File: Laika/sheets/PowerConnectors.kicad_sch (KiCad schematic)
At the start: 0 parts

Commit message: Created USB-C and XT30 Power Input Block
Created a power selection circuit that allows for providing system power
(VDD) via a USB-C receptacle (with ESD protection) or via a XT30
connector. Also attached pin headers to provide power from a bench when
doing bringup.
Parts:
- added D1, D2: D, symbol Device:D
- added J1: USB_C_Receptacle_USB2.0_16P, symbol Connector:USB_C_Receptacle_USB2.0_16P
- added J2: Conn_01x02_Socket, Connector_AMASS:AMASS_XT30PW-F_1x02_P2.50mm_Horizontal, symbol Connector:Conn_01x02_Socket
- added J3: Conn_01x02_Socket, Connector_PinHeader_1.00mm:PinHeader_1x02_P1.00mm_Vertical, symbol Connector:Conn_01x02_Socket
- added R1, R2: 5.1k, symbol Device:R
- added TP1: USB TP, TestPoint:TestPoint_Pad_1.0x1.0mm, symbol Connector:TestPoint
- added TP2: VDD TP, TestPoint:TestPoint_Pad_1.0x1.0mm, symbol Connector:TestPoint
- added TP3: VIN TP, TestPoint:TestPoint_Pad_1.0x1.0mm, symbol Connector:TestPoint
- added U1: USBLC6-2SC6, Package_TO_SOT_SMD:SOT-23-6, symbol Power_Protection:USBLC6-2SC6
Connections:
- new net: J1.A5 (CC1), R2.1
- new net: J1.A6 (D+), J1.B6 (D+), U1.3 (I/O2)
- new net: J1.A7 (D-), J1.B7 (D-), U1.1 (I/O1)
- new net: J1.B5 (CC2), R1.1
- new net GND: J1.A1 (GND), J1.A12 (GND), J1.B1 (GND), J1.B12 (GND), J1.S1 (SHIELD), J2.1 (Pin_1), J3.1 (Pin_1), R1.2, R2.2, U1.2 (GND)
- new net USB_DM: U1.6 (I/O1)
- new net USB_DP: U1.4 (I/O2)
- new net VBUS: D1.2 (A), J1.A4 (VBUS), J1.A9 (VBUS), J1.B4 (VBUS), J1.B9 (VBUS), TP1.1, U1.5 (VBUS)
- new net VDD: D1.1 (K), D2.1 (K), TP2.1
- new net VIN: D2.2 (A), J2.2 (Pin_2), J3.2 (Pin_2), TP3.1
- no-connect marks 0 -> 2
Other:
- note added: "Diode OR'ing between USB-C (VBUS) and XT30 (VIN)"
- note added: "Pin Header"
- note added: "Power Connectors"
- note added: "Power Selection"
- note added: "USB-C Receptacle"
- note added: "XT30"
- note added: "XT30 Power Connector"

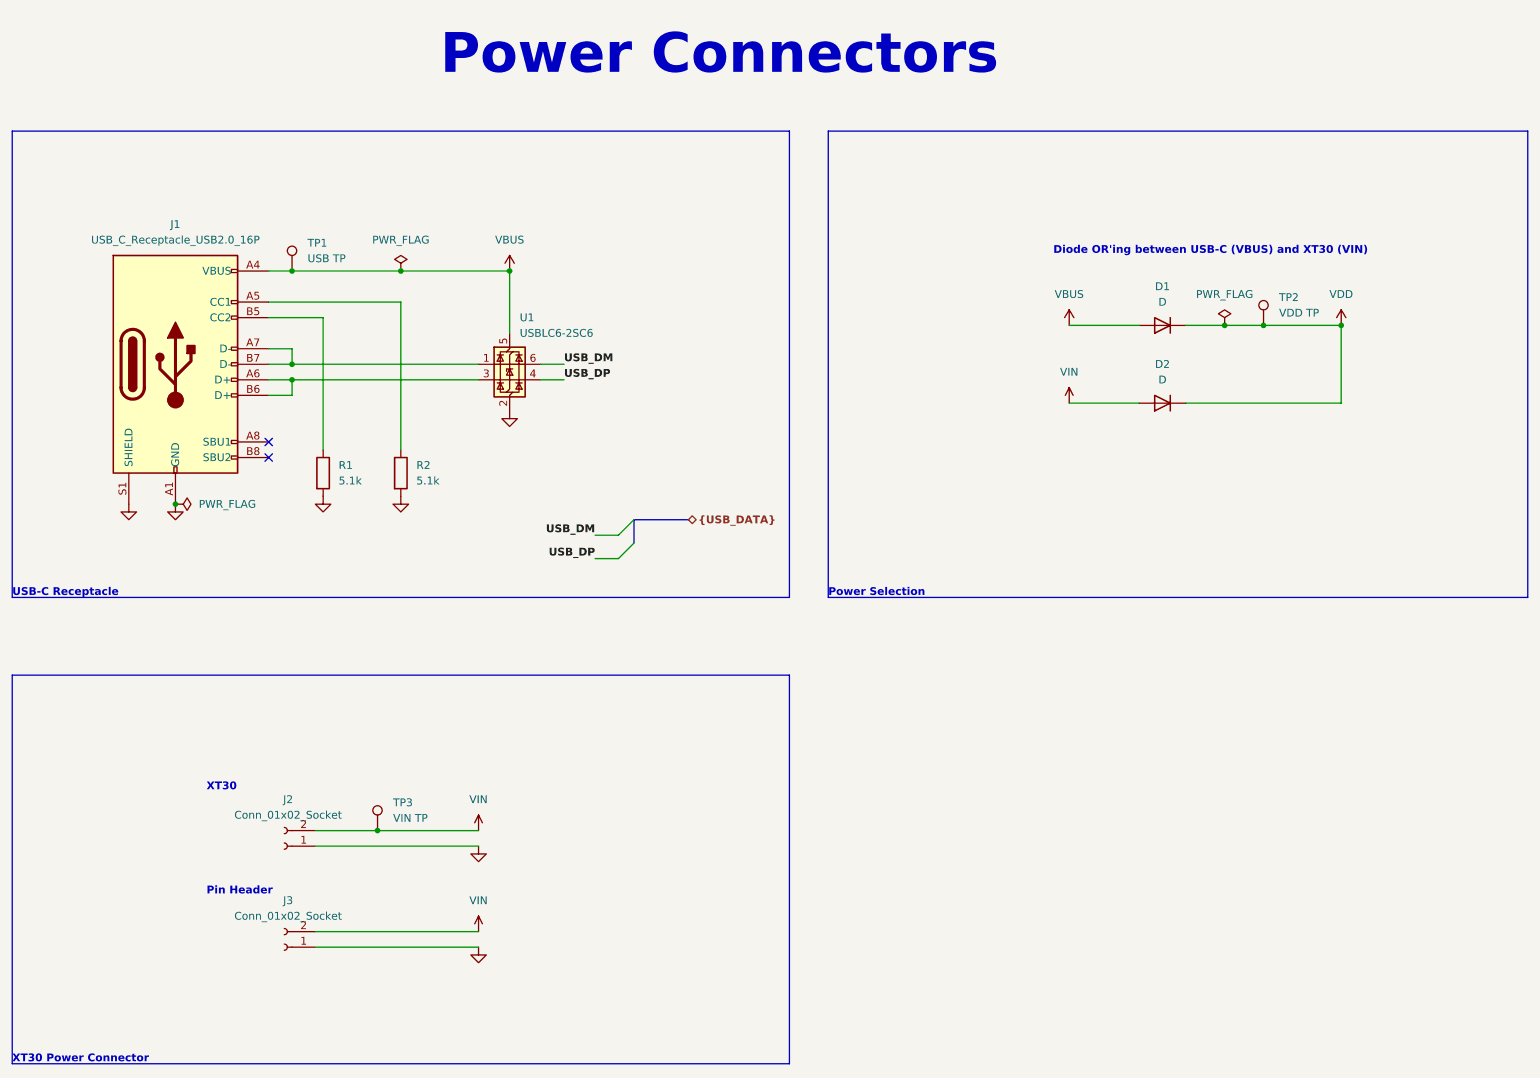
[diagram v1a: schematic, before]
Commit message: Connected USB data in schematic, adjusted Project Architecture
Adjusted the Project Architecture sheet and connected USB between the
Power Connector and SoC sheet. Cleaned up look of the Project
Architecture sheet. Added submodules for Milk V symbols and footprints.
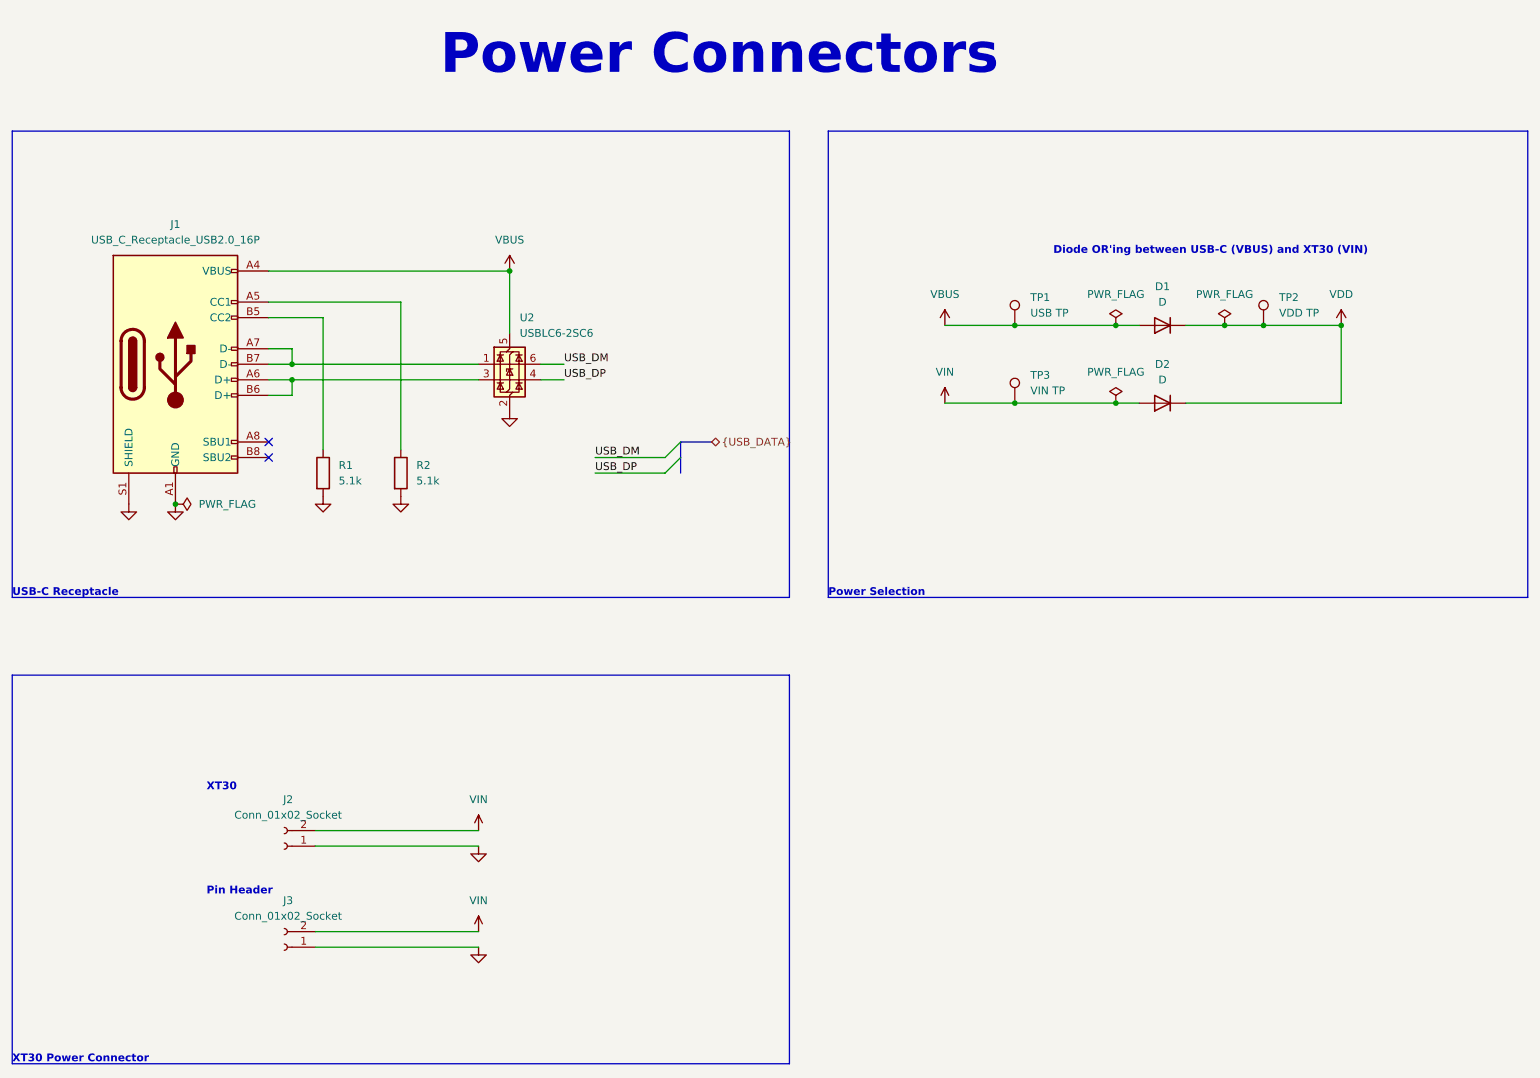
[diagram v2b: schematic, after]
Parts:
- renumbered U1 to U2
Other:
- moved on the sheet: TP1, TP3

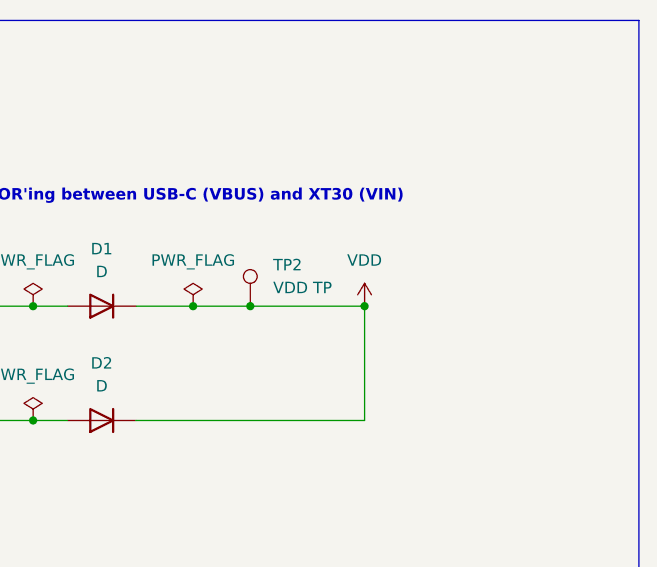
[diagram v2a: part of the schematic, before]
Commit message: Created 3.3V Buck Regulator Circuit
Created schematic for a 3.3V buck regulator. All component selection and
calaculation was performed using TI WEBENCH Power designer, of which the
artifacts are stored in 'calc'. Created Netclasses for PWR and USB.
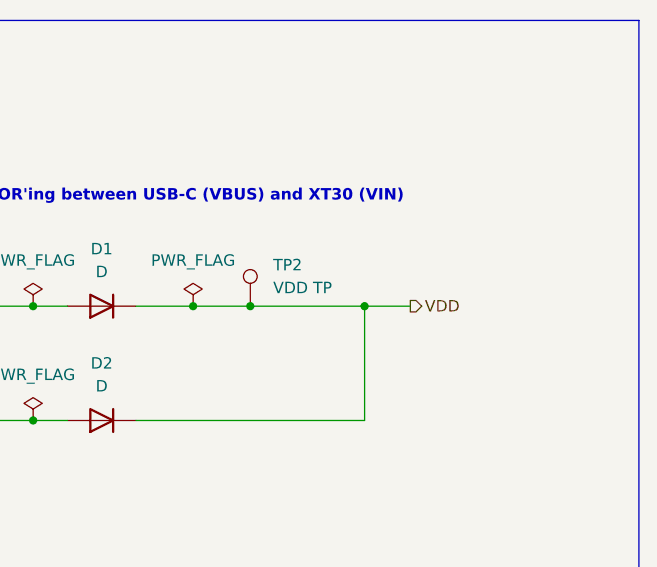
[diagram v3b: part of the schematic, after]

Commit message: Created 1.8V LDO circuit, assigned Mfr Part Numbers to Power IC's
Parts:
- U2: Manafacturer (none) -> STMicroelectronics; Part Number (none) -> USBLC6-2SC6
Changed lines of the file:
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@@
 			)
 		)
-		(property "Part Number" ""
+		(property "Part Number" "USBLC6-2SC6"
 			(at 106.68 76.2 0)
 			(effects
@@
 			)
 		)
-		(property "Manafacturer" ""
+		(property "Manafacturer" "STMicroelectronics"
 			(at 106.68 76.2 0)
 			(effects

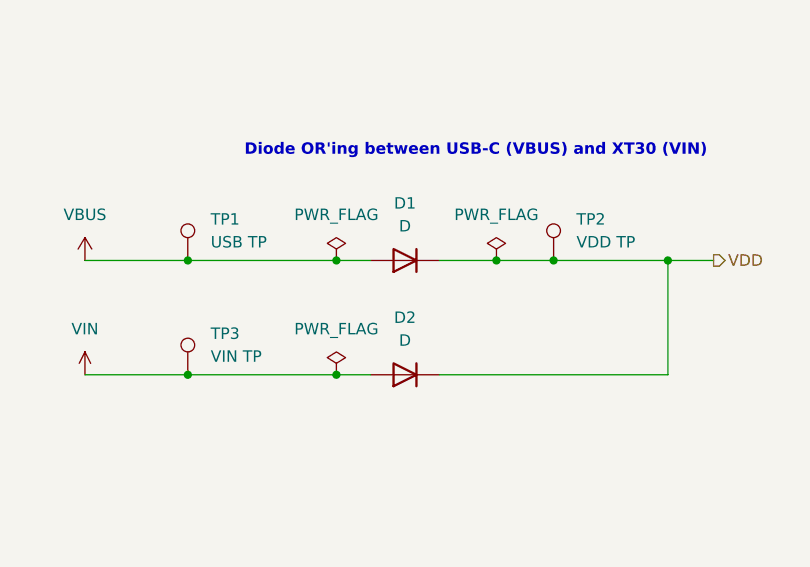
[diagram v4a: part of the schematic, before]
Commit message: Populated BOM with part numbers and footprints
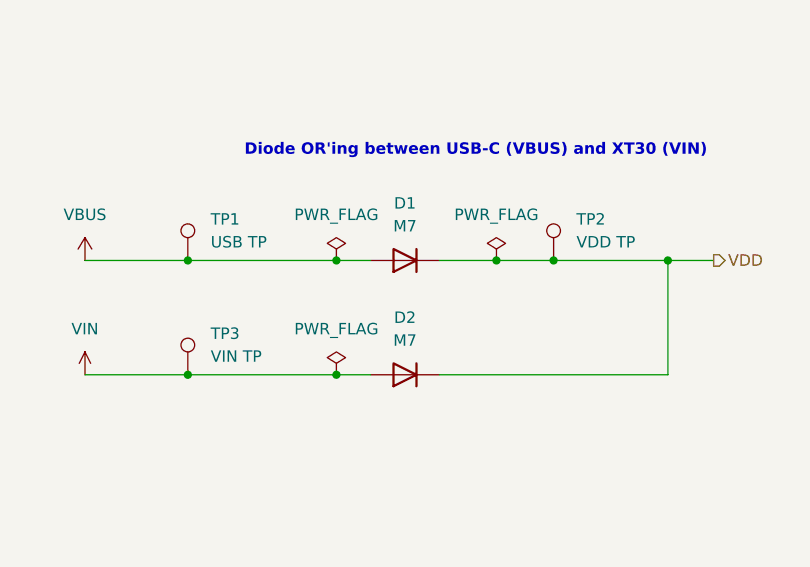
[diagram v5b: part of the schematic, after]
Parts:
- D1, D2: value D -> M7; footprint (none) -> Diode_SMD:D_SMA; JLC Part Type (none) -> Basic; Manafacturer (none) -> Diotec Semiconductor; Part Number (none) -> M7
- J1: footprint (none) -> Connector_USB:USB_C_Receptacle_GCT_USB4110; JLC Part Type (none) -> Extended; Manafacturer (none) -> Global Connector Technology; Part Number (none) -> USB4110-GF-A
- R1, R2: footprint (none) -> Capacitor_SMD:C_0402_1005Metric; JLC Part Type (none) -> Basic; Manafacturer (none) -> Royalohm; Part Number (none) -> 0402WGF5101TCE
- U2: JLC Part Type (none) -> Extended
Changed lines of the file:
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@@
 			)
 		)
-		(property "Footprint" ""
+		(property "Footprint" "Connector_USB:USB_C_Receptacle_GCT_USB4110"
 			(at 55.88 76.2 0)
 			(effects
@@
 			)
 		)
-		(property "JLC Part Type" ""
+		(property "JLC Part Type" "Extended"
 			(at 52.07 76.2 0)
 			(effects
@@
 			)
 		)
-		(property "Part Number" ""
+		(property "Part Number" "USB4110-GF-A "
 			(at 52.07 76.2 0)
 			(effects
@@
 			)
 		)
-		(property "Manafacturer" ""
+		(property "Manafacturer" "Global Connector Technology"
 			(at 52.07 76.2 0)
 			(effects
@@
 			)
 		)
-		(property "JLC Part Type" ""
+		(property "JLC Part Type" "Extended"
 			(at 106.68 76.2 0)
 			(effects
@@
 			)
 		)
-		(property "Value" "D"
+		(property "Value" "M7"
 			(at 213.36 78.74 0)
 			(effects
@@
 			)
 		)
-		(property "Footprint" ""
+		(property "Footprint" "Diode_SMD:D_SMA"
 			(at 213.36 82.55 0)
 			(effects
@@
 			)
 		)
-		(property "Datasheet" "~"
+		(property "Datasheet" "https://diotec.com/request/datasheet/m1.pdf"
 			(at 213.36 82.55 0)
 			(effects
@@
 			)
 		)
-		(property "JLC Part Type" ""
+		(property "JLC Part Type" "Basic"
 			(at 213.36 82.55 0)
 			(effects
@@
 			)
 		)
-		(property "Part Number" ""
+		(property "Part Number" "M7"
 			(at 213.36 82.55 0)
 			(effects
@@
 			)
 		)
-		(property "Manafacturer" ""
+		(property "Manafacturer" "Diotec Semiconductor"
 			(at 213.36 82.55 0)
 			(effects
@@
 			)
 		)
-		(property "Value" "D"
+		(property "Value" "M7"
 			(at 213.36 66.04 0)
 			(effects
@@
 			)
 		)
-		(property "Footprint" ""
+		(property "Footprint" "Diode_SMD:D_SMA"
 			(at 213.36 69.85 0)
 			(effects
@@
 			)
 		)
-		(property "Datasheet" "~"
+		(property "Datasheet" "https://diotec.com/request/datasheet/m1.pdf"
 			(at 213.36 69.85 0)
 			(effects
@@
 			)
 		)
-		(property "JLC Part Type" ""
+		(property "JLC Part Type" "Basic"
 			(at 213.36 69.85 0)
 			(effects
@@
 			)
 		)
-		(property "Part Number" ""
+		(property "Part Number" "M7"
 			(at 213.36 69.85 0)
 			(effects
@@
 			)
 		)
-		(property "Manafacturer" ""
+		(property "Manafacturer" "Diotec Semiconductor"
 			(at 213.36 69.85 0)
 			(effects
@@
 			)
 		)
-		(property "Footprint" ""
+		(property "Footprint" "Capacitor_SMD:C_0402_1005Metric"
 			(at 87.122 93.98 90)
 			(effects
@@
 			)
 		)
-		(property "Datasheet" "~"
+		(property "Datasheet" "https://www.mouser.com/datasheet/3/5925/1/1.pdf"
 			(at 88.9 93.98 0)
 			(effects
@@
 			)
 		)
-		(property "JLC Part Type" ""
+		(property "JLC Part Type" "Basic"
 			(at 88.9 93.98 0)
 			(effects
@@
 			)
 		)
-		(property "Part Number" ""
+		(property "Part Number" "0402WGF5101TCE"
 			(at 88.9 93.98 0)
 			(effects
@@
 			)
 		)
-		(property "Manafacturer" ""
+		(property "Manafacturer" "Royalohm"
 			(at 88.9 93.98 0)
 			(effects
@@
 			)
 		)
-		(property "Footprint" ""
+		(property "Footprint" "Capacitor_SMD:C_0402_1005Metric"
 			(at 74.422 93.98 90)
 			(effects
@@
 			)
 		)
-		(property "Datasheet" "~"
+		(property "Datasheet" "https://www.mouser.com/datasheet/3/5925/1/1.pdf"
 			(at 76.2 93.98 0)
 			(effects
@@
 			)
 		)
-		(property "JLC Part Type" ""
+		(property "JLC Part Type" "Basic"
 			(at 76.2 93.98 0)
 			(effects
@@
 			)
 		)
-		(property "Part Number" ""
+		(property "Part Number" "0402WGF5101TCE"
 			(at 76.2 93.98 0)
 			(effects
@@
 			)
 		)
-		(property "Manafacturer" ""
+		(property "Manafacturer" "Royalohm"
 			(at 76.2 93.98 0)
 			(effects

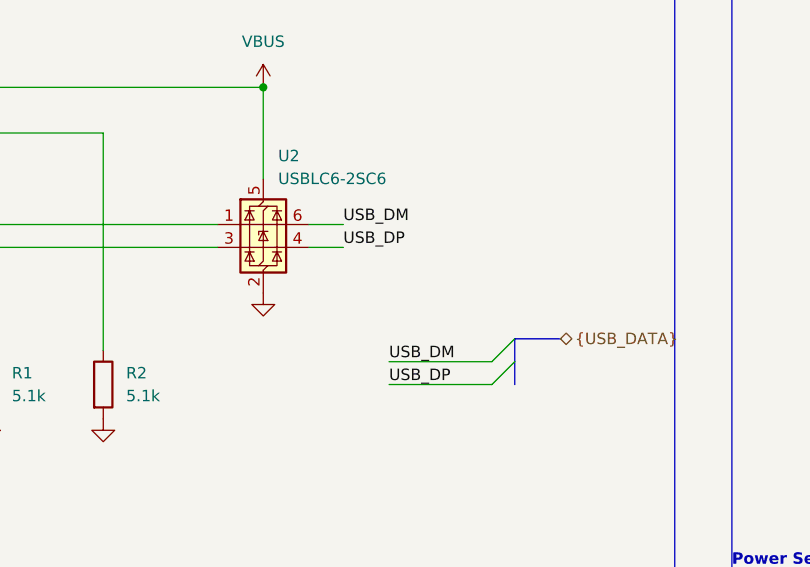
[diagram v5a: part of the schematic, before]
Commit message: Rename USB_DM to USB_DN
Matches KiCad Differential Naming Conventian
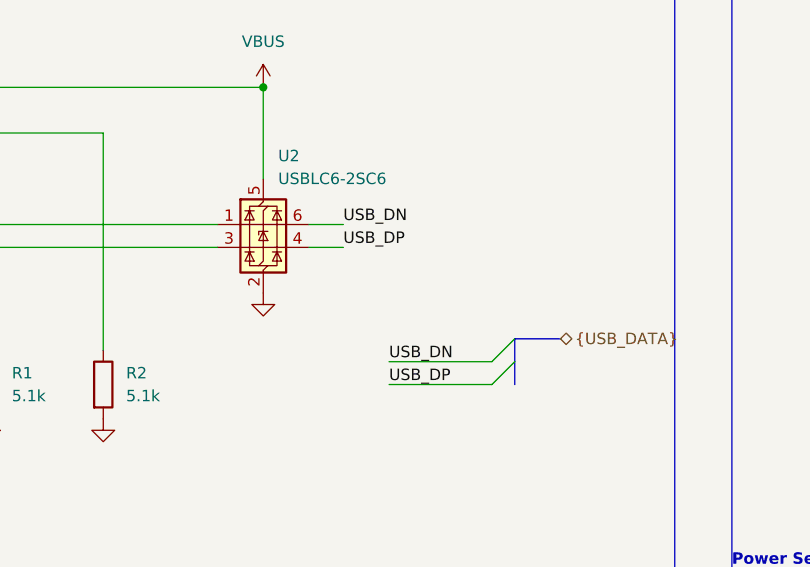
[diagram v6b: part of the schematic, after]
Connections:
- net USB_DM renamed USB_DN
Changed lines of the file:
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@@
 		)
 	)
-	(label "USB_DM"
+	(label "USB_DN"
 		(at 115.57 76.2 0)
 		(effects
@@
 		)
 	)
-	(label "USB_DM"
+	(label "USB_DN"
 		(at 120.65 91.44 0)
 		(effects
